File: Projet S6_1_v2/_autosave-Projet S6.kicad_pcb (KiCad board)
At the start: 2 copper layers, 143 x 20 mm, 26 parts, among them J101 Conn_01x02, J3 Conn_01x04_Socket

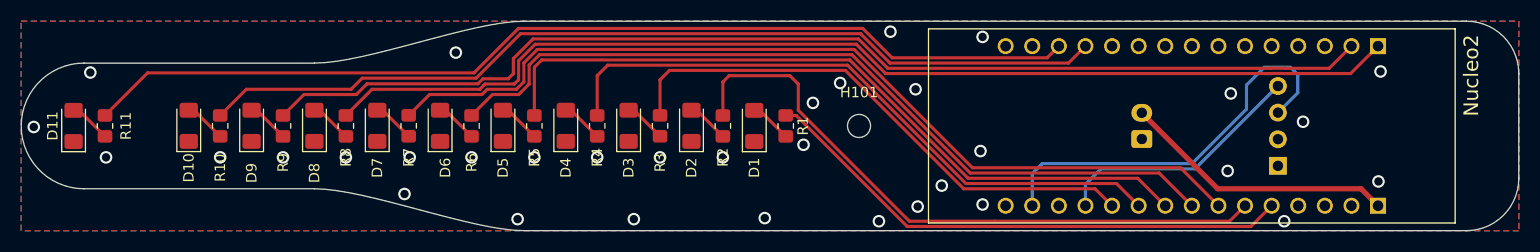
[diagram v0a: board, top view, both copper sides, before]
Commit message: Correction du Timer et clignotement des LEDs
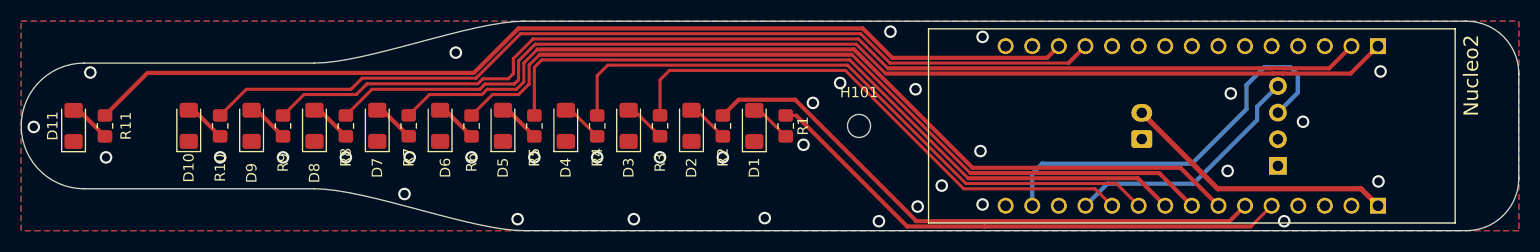
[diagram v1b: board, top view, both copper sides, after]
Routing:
- net LED 2: track 61.1 -> 56.0 mm
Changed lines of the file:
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@@
 			(drillshape 0)
 			(scaleselection 1)
-			(outputdirectory "gerber/")
+			(outputdirectory "Gerber_final/")
 		)
 	)
@@
 		(start 99 71)
 		(end 96 68)
-		(width 0.3)
+		(width 0.4)
 		(layer "F.Cu")
 		(net 6)
@@
 		(start 93 71)
 		(end 90 68)
-		(width 0.3)
+		(width 0.4)
 		(layer "F.Cu")
 		(net 7)
@@
 		(start 87 70.9875)
 		(end 84 67.9875)
-		(width 0.3)
+		(width 0.4)
 		(layer "F.Cu")
 		(net 8)
@@
 		(start 81 71)
 		(end 78 68)
-		(width 0.3)
+		(width 0.4)
 		(layer "F.Cu")
 		(net 9)
@@
 		(start 75 71)
 		(end 72 68)
-		(width 0.3)
+		(width 0.4)
 		(layer "F.Cu")
 		(net 10)
@@
 		(start 69 71)
 		(end 66 68)
-		(width 0.3)
+		(width 0.4)
 		(layer "F.Cu")
 		(net 11)
@@
 		(start 58 71)
 		(end 55 68)
-		(width 0.3)
+		(width 0.4)
 		(layer "F.Cu")
 		(net 12)
@@
 		(start 167.421026 79.598974)
 		(end 142 79.598985)
-		(width 0.3)
+		(width 0.4)
 		(layer "F.Cu")
 		(net 13)
@@
 		(start 134.598985 79.598985)
 		(end 124 69)
-		(width 0.3)
+		(width 0.4)
 		(layer "F.Cu")
 		(net 13)
@@
 		(start 142 79.598985)
 		(end 134.598985 79.598985)
-		(width 0.3)
+		(width 0.4)
 		(layer "F.Cu")
 		(net 13)
@@
 	)
 	(segment
-		(start 124.2 66)
-		(end 123.4 65.2)
-		(width 0.3)
-		(layer "F.Cu")
-		(net 14)
-	)
-	(segment
-		(start 124.2 68.49148)
-		(end 124.2 66)
-		(width 0.3)
+		(start 118.501 67.499)
+		(end 123.899 67.499)
+		(width 0.4)
 		(layer "F.Cu")
 		(net 14)
@@
 		(start 166.86 77.62)
 		(end 165.382025 79.097975)
-		(width 0.3)
+		(width 0.4)
 		(layer "F.Cu")
 		(net 14)
@@
 	(segment
 		(start 143 79.097984)
-		(end 134.806504 79.097984)
-		(width 0.3)
+		(end 135.4 79.097984)
+		(width 0.4)
 		(layer "F.Cu")
 		(net 14)
 	)
 	(segment
-		(start 123.4 65.2)
-		(end 117.6 65.2)
-		(width 0.3)
+		(start 135.4 79)
+		(end 135.4 79.097984)
+		(width 0.2)
 		(layer "F.Cu")
 		(net 14)
 	)
 	(segment
-		(start 117.6 65.2)
-		(end 117 65.8)
-		(width 0.3)
+		(start 123.899 67.499)
+		(end 135.4 79)
+		(width 0.4)
 		(layer "F.Cu")
 		(net 14)
@@
 		(start 165.382025 79.097975)
 		(end 143 79.097984)
-		(width 0.3)
-		(layer "F.Cu")
-		(net 14)
-	)
-	(segment
-		(start 134.806504 79.097984)
-		(end 124.2 68.49148)
-		(width 0.3)
+		(width 0.4)
 		(layer "F.Cu")
 		(net 14)
 	)
 	(segment
-		(start 117 65.8)
-		(end 117 69)
-		(width 0.3)
+		(start 117 69)
+		(end 118.501 67.499)
+		(width 0.4)
 		(layer "F.Cu")
 		(net 14)
@@
 		(start 156.618 74.998)
 		(end 140.41504 74.998)
-		(width 0.3)
+		(width 0.4)
 		(layer "F.Cu")
 		(net 17)
@@
 		(start 159.24 77.62)
 		(end 156.618 74.998)
-		(width 0.3)
+		(width 0.4)
 		(layer "F.Cu")
 		(net 17)
@@
 		(start 158.657 74.497)
 		(end 161.78 77.62)
-		(width 0.3)
+		(width 0.4)
 		(layer "F.Cu")
 		(net 18)
@@
 		(start 99.495479 63.196)
 		(end 129.32156 63.196)
-		(width 0.3)
+		(width 0.4)
 		(layer "F.Cu")
 		(net 18)
@@
 		(start 140.62256 74.497)
 		(end 158.657 74.497)
-		(width 0.3)
+		(width 0.4)
 		(layer "F.Cu")
 		(net 18)
@@
 		(start 160.696 73.996)
 		(end 140.83008 73.996)
-		(width 0.3)
+		(width 0.4)
 		(layer "F.Cu")
 		(net 19)
@@
 		(start 140.83008 73.996)
 		(end 129.52908 62.695)
-		(width 0.3)
+		(width 0.4)
 		(layer "F.Cu")
 		(net 19)
@@
 		(start 164.32 77.62)
 		(end 160.696 73.996)
-		(width 0.3)
+		(width 0.4)
 		(layer "F.Cu")
 		(net 19)
@@
 		(start 129.52908 62.695)
 		(end 99.287957 62.695)
-		(width 0.3)
+		(width 0.4)
 		(layer "F.Cu")
 		(net 19)
@@
 		(start 132.5426 65)
 		(end 169.491528 65)
-		(width 0.3)
+		(width 0.4)
 		(layer "F.Cu")
 		(net 20)
@@
 		(start 176.94 65)
 		(end 179.56 62.38)
-		(width 0.3)
+		(width 0.4)
 		(layer "F.Cu")
 		(net 20)
@@
 		(start 169.502529 64.989)
 		(end 170.497471 64.989)
-		(width 0.3)
+		(width 0.4)
 		(layer "F.Cu")
 		(net 20)
@@
 		(start 170.508472 65.000001)
 		(end 176.94 65)
-		(width 0.3)
+		(width 0.4)
 		(layer "F.Cu")
 		(net 20)
@@
 		(start 170.715992 64.499)
 		(end 174.901 64.499)
-		(width 0.3)
+		(width 0.4)
 		(layer "F.Cu")
 		(net 21)
@@
 		(start 132.75012 64.499)
 		(end 169.284008 64.499)
-		(width 0.3)
+		(width 0.4)
 		(layer "F.Cu")
 		(net 21)
@@
 		(start 169.295009 64.488)
 		(end 170.704991 64.488)
-		(width 0.3)
+		(width 0.4)
 		(layer "F.Cu")
 		(net 21)
@@
 		(start 174.901 64.499)
 		(end 177.02 62.38)
-		(width 0.3)
+		(width 0.4)
 		(layer "F.Cu")
 		(net 21)
@@
 		(start 150.002 63.998)
 		(end 151.62 62.38)
-		(width 0.3)
+		(width 0.4)
 		(layer "F.Cu")
 		(net 22)
@@
 		(start 93.2297 64.936219)
 		(end 97.474919 60.691)
-		(width 0.3)
+		(width 0.4)
 		(layer "F.Cu")
 		(net 23)
@@
 		(start 97.474919 60.691)
 		(end 130.35916 60.691)
-		(width 0.3)
+		(width 0.4)
 		(layer "F.Cu")
 		(net 23)
@@
 		(start 130.35916 60.691)
 		(end 133.16416 63.496)
-		(width 0.3)
+		(width 0.4)
 		(layer "F.Cu")
 		(net 23)
@@
 		(start 133.16416 63.496)
 		(end 147.964 63.496)
-		(width 0.3)
+		(width 0.4)
 		(layer "F.Cu")
 		(net 23)
@@
 		(start 58 69)
 		(end 62.063781 64.936219)
-		(width 0.3)
+		(width 0.4)
 		(layer "F.Cu")
 		(net 23)
@@
 		(start 62.063781 64.936219)
 		(end 93.2297 64.936219)
-		(width 0.3)
+		(width 0.4)
 		(layer "F.Cu")
 		(net 23)
@@
 		(start 147.964 63.496)
 		(end 149.08 62.38)
-		(width 0.3)
+		(width 0.4)
 		(layer "F.Cu")
 		(net 23)
 	)
 	(segment
-		(start 151.62 75.58)
-		(end 151.62 77.62)
-		(width 0.3)
+		(start 168.01 69.44)
+		(end 161.94 75.51)
+		(width 0.4)
 		(layer "B.Cu")
 		(net 25)
 	)
 	(segment
-		(start 153.1 74.1)
-		(end 151.62 75.58)
-		(width 0.3)
+		(start 168.01 68.18)
+		(end 168.01 69.44)
+		(width 0.4)
 		(layer "B.Cu")
 		(net 25)
 	)
 	(segment
-		(start 170 66.19)
-		(end 162.09 74.1)
-		(width 0.3)
+		(start 161.94 75.51)
+		(end 153.73 75.51)
+		(width 0.4)
 		(layer "B.Cu")
 		(net 25)
 	)
 	(segment
-		(start 162.09 74.1)
-		(end 153.1 74.1)
-		(width 0.3)
+		(start 153.73 75.51)
+		(end 151.62 77.62)
+		(width 0.4)
+		(layer "B.Cu")
+		(net 25)
+	)
+	(segment
+		(start 170 66.19)
+		(end 168.01 68.18)
+		(width 0.4)
 		(layer "B.Cu")
 		(net 25)
@@
 		(start 161.801 73.599)
 		(end 147.501 73.599)
-		(width 0.3)
+		(width 0.4)
 		(layer "B.Cu")
 		(net 26)
@@
 		(start 167 68.4)
 		(end 161.801 73.599)
-		(width 0.3)
+		(width 0.4)
 		(layer "B.Cu")
 		(net 26)
@@
 		(start 147.501 73.599)
 		(end 146.54 74.56)
-		(width 0.3)
+		(width 0.4)
 		(layer "B.Cu")
 		(net 26)
@@
 		(start 170 68.73)
 		(end 171.9 66.83)
-		(width 0.3)
+		(width 0.4)
 		(layer "B.Cu")
 		(net 26)
@@
 		(start 146.54 74.56)
 		(end 146.54 77.62)
-		(width 0.3)
+		(width 0.4)
 		(layer "B.Cu")
 		(net 26)
@@
 		(start 168.7 64.4)
 		(end 167 66.1)
-		(width 0.3)
+		(width 0.4)
 		(layer "B.Cu")
 		(net 26)
@@
 		(start 167 66.1)
 		(end 167 68.4)
-		(width 0.3)
+		(width 0.4)
 		(layer "B.Cu")
 		(net 26)
@@
 		(start 171.9 65.1)
 		(end 171.2 64.4)
-		(width 0.3)
+		(width 0.4)
 		(layer "B.Cu")
 		(net 26)
@@
 		(start 171.9 66.83)
 		(end 171.9 65.1)
-		(width 0.3)
+		(width 0.4)
 		(layer "B.Cu")
 		(net 26)
@@
 		(start 171.2 64.4)
 		(end 168.7 64.4)
-		(width 0.3)
+		(width 0.4)
 		(layer "B.Cu")
 		(net 26)
